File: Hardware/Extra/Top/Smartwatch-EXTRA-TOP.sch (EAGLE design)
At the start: 69 parts, among them SW6 SWITCH.MOM, SW7 SWITCH.MOM, U2 NRF52832_MODULE_MDBT42, U4 FT231XS, U5 PHOTOTRANSISTOR

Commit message: Extra features updated
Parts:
- removed C25: 1u, LinnesLab-Passives:CAPACITOR0603
- removed C26: 100n, LinnesLab-Passives:CAPACITOR0603
- removed D4: (no value), LinnesLab-DiscreteSemi:SCHOTTKY-USC
- removed LED5: RED, LinnesLab-LED:LED0603
- removed LED6: YELLOW, LinnesLab-LED:LED0603
- removed Q1: (no value), LinnesLab-DiscreteSemi:NFET-AO3404A
- removed R17: 1k, LinnesLab-Passives:RESISTOR0603
- removed SW6, SW7: SWITCH.MOM, LinnesLab-Switches:SWITCH.MOM
- removed U4: FT231XS, LinnesLab-DigitalIC:FT231XS
- added C2: 10u, LinnesLab-Passives:CAPACITOR0805
- added C27: 10p, LinnesLab-Passives:CAPACITOR0603
- added C28: 1u, LinnesLab-Passives:CAPACITOR0603
- added C29: 100n, LinnesLab-Passives:CAPACITOR0603
- added D3: (no value), LinnesLab-DiscreteSemi:SCHOTTKY-USC
- added J3: (no value), LinnesLab-Connectors:CONN_041.27MM
- added LED1: RED, LinnesLab-LED:LED0603
- added LED2: BLUE, LinnesLab-LED:LED0603
- added MIC1: (no value), LinnesLab-Electromechanical:MICROPHONE_CMC-5042PF-AC.CMEJ-0415-42-P
- added Q2: (no value), LinnesLab-DiscreteSemi:NPN-GENERIC
- added Q3: (no value), LinnesLab-DiscreteSemi:NFET-AO3404A
- added R21: 100k, LinnesLab-Passives:RESISTOR0603
- added R22, R23, R26: 10k, LinnesLab-Passives:RESISTOR0603
- added R9: 27, LinnesLab-Passives:RESISTOR0603
- added U1: NRF52832_MODULE_MDBT42, LinnesLab-Microcontrollers:NRF52832_MODULE_MDBT42
- added U6: MCP9808-MSOP8, LinnesLab-Sensors:MCP9808-MSOP8
- C1: value 4.7u -> 1u
- C10, C11: value 300p -> 2.2uF; device LinnesLab-Passives:CAPACITOR0603 -> LinnesLab-Passives:CAPACITOR0402
- C12: value 10u -> 2.2uF; device LinnesLab-Passives:CAPACITOR0805 -> LinnesLab-Passives:CAPACITOR0402
- C13, C18: value 2.2uF -> 100n; device LinnesLab-Passives:CAPACITOR0402 -> LinnesLab-Passives:CAPACITOR0603
- C14: value 100n -> 4.7u
- C15, C17: value 2.2uF -> 47p; device LinnesLab-Passives:CAPACITOR0402 -> LinnesLab-Passives:CAPACITOR0603
- C16: value 10uF -> 1u
- C19: value 2.2uF -> 1u; device LinnesLab-Passives:CAPACITOR0402 -> LinnesLab-Passives:CAPACITOR0603
- C20: value 2.2u -> 4.7u
- C22: value 47p -> 2.2u
- C23: value 47p -> 100n
- C24: value 10p -> 100n
- C3: value 4.7u -> (none)
- C4: value 100n -> (none)
- C5, C6: value 1u -> 300p
- C7: value 1u -> 10uF
- C8, C9: value (none) -> 2.2uF; device LinnesLab-Passives:CAPACITOR0603 -> LinnesLab-Passives:CAPACITOR0402
- J1: device LinnesLab-Connectors:CONN_07 -> LinnesLab-Connectors:CONN_07-1.27MM
- LED4: value BLUE -> YELLOW
- R11: value (none) -> 4.7k
- R15: value 10k -> 1k
- R16: value 27 -> 1k
- R18: value 1k -> 10k
- R6: value 10k -> 390k
- R7: value 390k -> 10k
- U2: value NRF52832_MODULE_MDBT42 -> (none); device LinnesLab-Microcontrollers:NRF52832_MODULE_MDBT42 -> LinnesLab-Displays:DISP_OLED_UG-2864HSWEG01-NO-WRAPAROUND
- U3: value (none) -> FT231XS; device LinnesLab-Displays:DISP_OLED_UG-2864HSWEG01-NO-WRAPAROUND -> LinnesLab-DigitalIC:FT231XS
- renumbered CHRG2 to CHRG1, CORTEX1 to DEBUG1, JP2 to JP1, L2 to L1, LDO2 to LDO1, SW3 to SW1, USB2 to USB1, XTAL2 to XTAL1
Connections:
- removed net A0/LIGHT: C20.1, R19.2, U2.P0.02/AIN0, U5.E
- removed net D11/SW1: SW7.1, U2.P0.11
- removed net D15/SW2: SW6.1, U2.P0.15
- removed net D29/LED.CTRL: J1.6, U2.P0.29/AIN5
- removed net D5/MOTOR: Q1.G, R15.2, U2.P0.05/AIN3
- removed net N$21: SW7.3, SW7.4
- removed net N$22: SW6.3, SW6.4
- new net A0/MICROPHONE: Q2.C, R21.2, R22.1, U1.P0.02/AIN0
- new net A5/LIGHT: C22.1, R18.2, U1.P0.29/AIN5, U5.E
- new net ALERT: R26.1, U6.ALERT
- new net D11/MOTOR: Q3.G, R19.2, U1.P0.11
- new net D15/LED.CTRL: J1.6, U1.P0.15
- new net D5/CD1: U1.P0.05/AIN3
- new net N$19: C23.1, MIC1.+, R23.1
- new net N$20: C23.2, Q2.B, R21.1
- net !CTS: now also U3.!CTS; no longer U4.!CTS
- net !DTR: now also U3.!DTR; no longer U4.!DTR
- net 3.3V: now also C11.2, C18.2, C19.1, C2.2, C24.1, C27.2, C28.1, C29.1, D5.C, J3.2, LED3.A, LED4.A, R12.2, R22.2, R23.2, R26.2, R7.2, U1.VDD, U2.VBAT, U3.!RESET, U3.VCCIO, U6.VDD; no longer C17.2, C19.2, C24.2, C25.1, C26.1, C4.2, C6.1, D2.C, LED5.A, LED6.A, R5.2, R8.2, U3.VBAT, U3.VDD, U4.!RESET, U4.VCCIO
- net A4/BATT: now also U1.P0.28/AIN4; no longer U2.P0.28/AIN4
- net A6/TIA: now also U1.P0.30/AIN6; no longer U2.P0.30/AIN6
- net A7/PPG: now also U1.P0.31/AIN7; no longer U2.P0.31/AIN7
- net D16/CS.OLED: now also U1.P0.16, U2./CS; no longer U2.P0.16, U3./CS
- net D27/CHRG.STAT: now also R8.1, U1.P0.27; no longer R12.1, U2.P0.27
- net D3/RESET.OLED: now also U1.P0.03/AIN1, U2./RES; no longer U2.P0.03/AIN1, U3./RES
- net D4/DC.OLED: now also U1.P0.04/AIN2, U2.DC/I2C_SA0; no longer U2.P0.04/AIN2, U3.DC/I2C_SA0
- net D7/SD.CS: now also U1.P0.07; no longer U2.P0.07
- net DFU: now also U1.P0.20; no longer U2.P0.20
- net DTR: now also C13.1; no longer C14.1
- net FRST: now also U1.P0.22; no longer U2.P0.22
- net FT3V3: now also U3.3V3OUT; no longer U4.3V3OUT
- net GND: now also C1.2, C11.1, C14.1, C15.1, C17.2, C19.2, C2.1, C24.2, C28.2, C29.2, C3.1, C4.2, C5.2, C7.1, C9.1, J3.1, LED1.C, LED2.C, MIC1.-, Q2.E, Q3.S, R12.1, R18.1, R5.1, R6.2, U1.GND@1, U1.GND@2, U1.GND@3, U1.GND@4, U2.BS0, U2.BS2, U2.NC(GND)@1, U2.NC(GND)@2, U2.VLSS, U2.VSS, U3.GND@16, U3.GND@6, U6.A0, U6.A1, U6.A2, U6.GND; no longer C1.1, C10.2, C11.2, C17.1, C19.1, C23.1, C25.2, C26.2, C3.2, C4.1, C5.1, C7.2, C8.1, C9.2, LED3.C, LED4.C, Q1.S, R15.1, R6.1, R7.2, R8.1, U2.GND@1, U2.GND@2, U2.GND@3, U2.GND@4, U3.BS0, U3.BS2, U3.NC(GND)@1, U3.NC(GND)@2, U3.VLSS, U3.VSS, U4.GND@16, U4.GND@6
- net LED1: now also U1.P0.17; no longer U2.P0.17
- net LED2: now also U1.P0.19; no longer U2.P0.19
- net MISO: now also U1.P0.14; no longer U2.P0.14
- net MOSI: now also U1.P0.13, U2.D1/SPI_SDIN/I2C_SDA; no longer U2.P0.13, U3.D1/SPI_SDIN/I2C_SDA
- net N$1: now also R5.2, U2.BS1; no longer R6.2, U3.BS1
- net N$10: now also LED2.A; no longer LED4.A
- net N$11: now also U1.DCC; no longer U2.DCC
- net N$12: now also C1.1, U1.DEC4; no longer C7.1, U2.DEC4
- net N$13: now also C7.2, U2.VCC; no longer C16.2, U3.VCC
- net N$15: now also C9.2, U2.VCOMH; no longer C18.2, U3.VCOMH
- net N$18: now also C27.1, D5.A, Q3.D; no longer C24.1, D2.A, Q1.D
- net N$2: now also R6.1, U2.IREF; no longer R7.1, U3.IREF
- net N$25: now also R9.2, U3.USBDM; no longer R10.2, U4.USBDM
- net N$26: now also R10.2, U3.USBDP; no longer R16.2, U4.USBDP
- net N$27: now also LED3.C, R15.2; no longer LED5.C, R17.2
- net N$28: now also LED4.C, R16.2; no longer LED6.C, R18.2
- net N$3: now also C10.2, U2.C2P; no longer C13.2, U3.C2P
- net N$4: now also C3.2, U1.P0.00/XL1; no longer C8.2, U2.P0.00/XL1
- net N$5: now also C10.1, U2.C2N; no longer C13.1, U3.C2N
- net N$6: now also C4.1, U1.P0.01/XL2; no longer C9.1, U2.P0.01/XL2
- net N$7: now also C8.2, U2.C1P; no longer C15.2, U3.C1P
- net N$8: now also C8.1, U2.C1N; no longer C15.1, U3.C1N
- net N$9: now also LED1.A; no longer LED3.A
- net P0.09/NFC1: now also C5.1, U1.P0.09; no longer C11.1, U2.P0.09
- net P0.10/NFC2: now also C6.1, U1.P0.10; no longer C10.1, U2.P0.10
- net RESET: now also C13.2, R7.1, U1.P0.21/RESET; no longer C14.2, R5.1, U2.P0.21/RESET
- net RXD: now also U1.P0.08, U3.RXD; no longer U2.P0.08, U4.RXD
- net RXLED: now also R15.1, U3.CBUS1; no longer R17.1, U4.CBUS1
- net SCK: now also U1.P0.12, U2.D0/SPI_SCLK/I2C_SCK; no longer U2.P0.12, U3.D0/SPI_SCLK/I2C_SCK
- net SCL: now also J3.3, U1.P0.26, U6.SCL; no longer U2.P0.26
- net SDA: now also J3.4, U1.P0.25, U6.SDA; no longer U2.P0.25
- net SWCLK: now also U1.SWDCLK; no longer U2.SWDCLK
- net SWDIO: now also U1.SWDIO; no longer U2.SWDIO
- net SWO: now also U1.P0.18/SWO; no longer U2.P0.18/SWO
- net TXD: now also U1.P0.06, U3.TXD; no longer U2.P0.06, U4.TXD
- net TXLED: now also R16.1, U3.CBUS2; no longer R18.1, U4.CBUS2
- net USB+: now also C17.1, R10.1; no longer C22.1, R16.1
- net USB-: now also C15.2, R9.1; no longer C23.2, R10.1
- net VIN: now also C14.2, C16.2, D2.C, D3.C, R8.2; no longer C1.2, C5.2, D4.C, D5.C, R12.2
- net VLIPO: now also C20.1, D2.A; no longer C3.1, D4.A
- net V_USB: now also D3.A, U3.VCC; no longer D5.A, U4.VCC
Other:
- note added: "I2C Adress: A0,A1,A2 connected to ground: 0x18 Other addresses: 0x19 to 0x1F"
- moved on the sheet: C1, C10, C11, C12, C13, C14, C15, C16, C17, C18, C19, C20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

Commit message: Extra Silkscreens updated
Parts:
- U1: SPICEPREFIX (none) -> X

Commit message: Microphone Removed,Silkscreen Updated, Bom Updated
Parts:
- removed C23: 100n, LinnesLab-Passives:CAPACITOR0603
- removed MIC1: (no value), LinnesLab-Electromechanical:MICROPHONE_CMC-5042PF-AC.CMEJ-0415-42-P
- removed Q2: (no value), LinnesLab-DiscreteSemi:NPN-GENERIC
- removed R21: 100k, LinnesLab-Passives:RESISTOR0603
- removed R22, R23: 10k, LinnesLab-Passives:RESISTOR0603
- added J4: (no value), LinnesLab-Connectors:CONN_03.50MIL
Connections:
- removed net A0/MICROPHONE: Q2.C, R21.2, R22.1, U1.P0.02/AIN0
- removed net D5/CD1: U1.P0.05/AIN3
- removed net D7/SD.CS: U1.P0.07
- removed net N$19: C23.1, MIC1.+, R23.1
- removed net N$20: C23.2, Q2.B, R21.1
- new net A.IN: J4.1, U1.P0.02/AIN0
- new net B.IN: J4.3, U1.P0.07
- new net MOM.BUTTON: J4.2, U1.P0.05/AIN3
- net 3.3V: no longer R22.2, R23.2
- net GND: no longer MIC1.-, Q2.E
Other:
- note added: "Ambient Light Sensor"
- note added: "Temperature Sensor"
- note added: "Vibration Motor"
- note removed: "Buttons"
- moved on the sheet: C22, C24, C27, C28, C29, D5, M1, Q3, R18, R19, R26, U5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

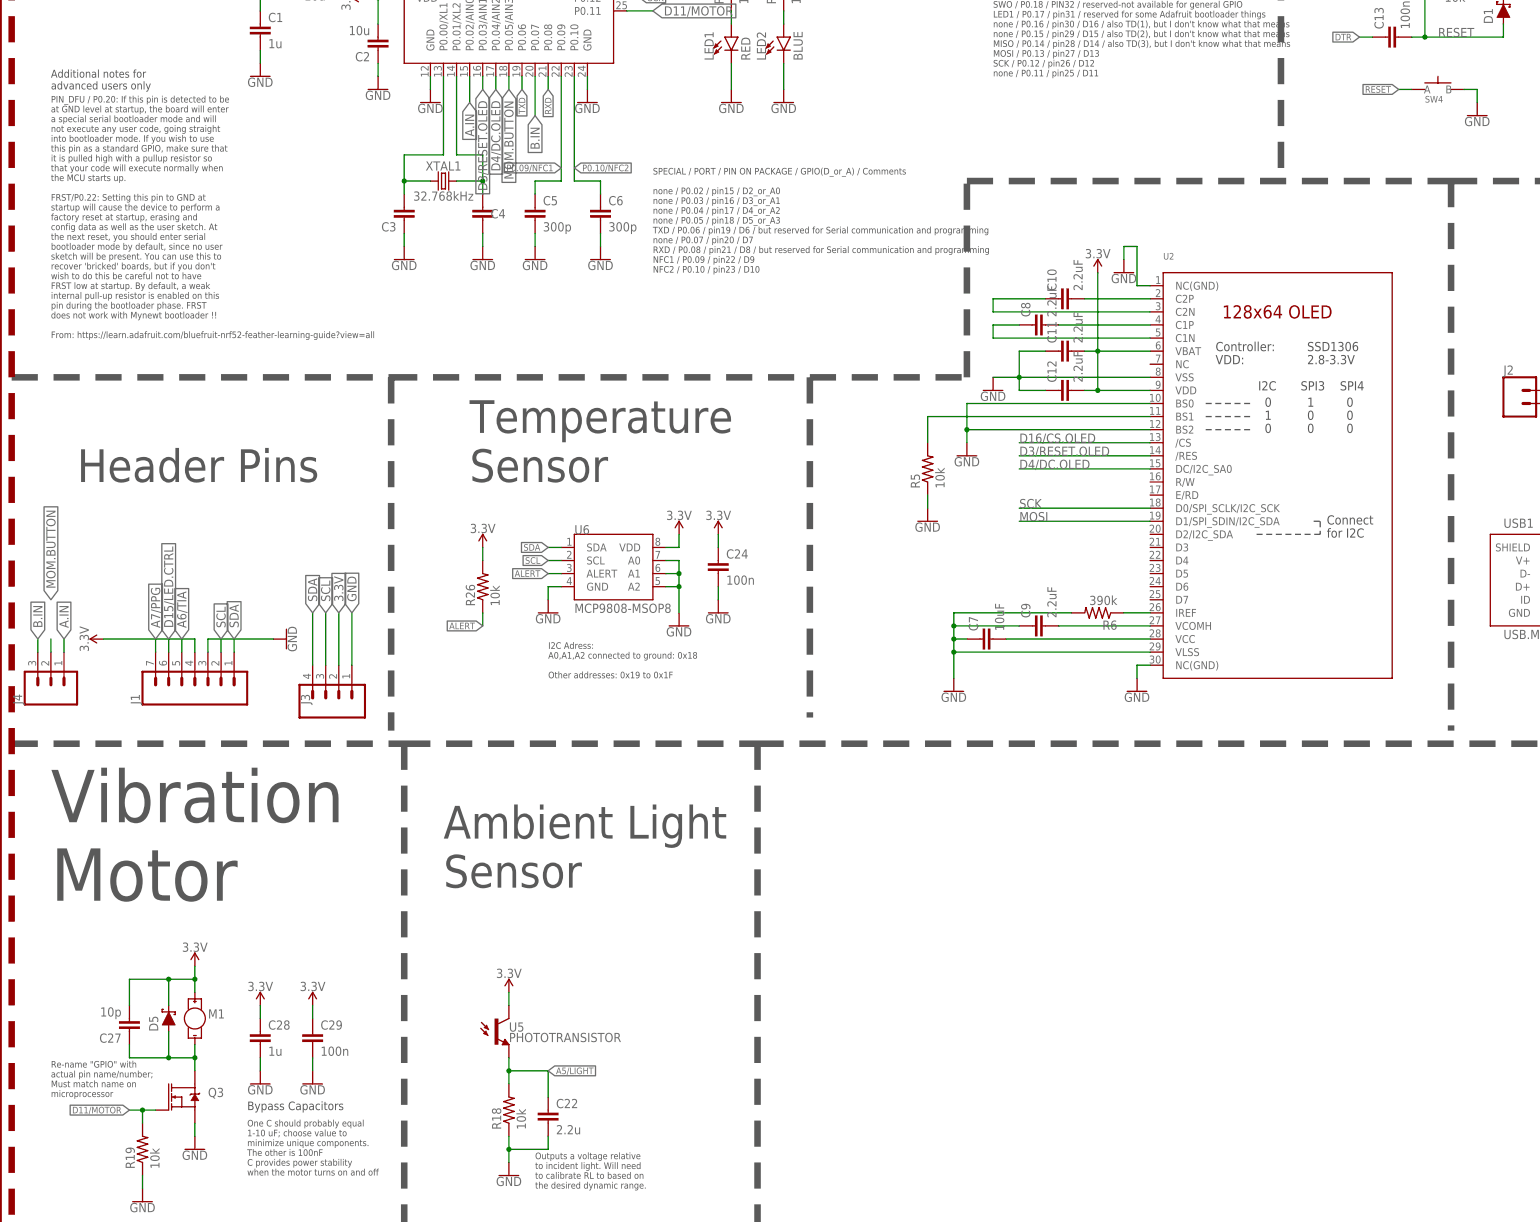
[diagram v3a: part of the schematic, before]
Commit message: BOMs finished
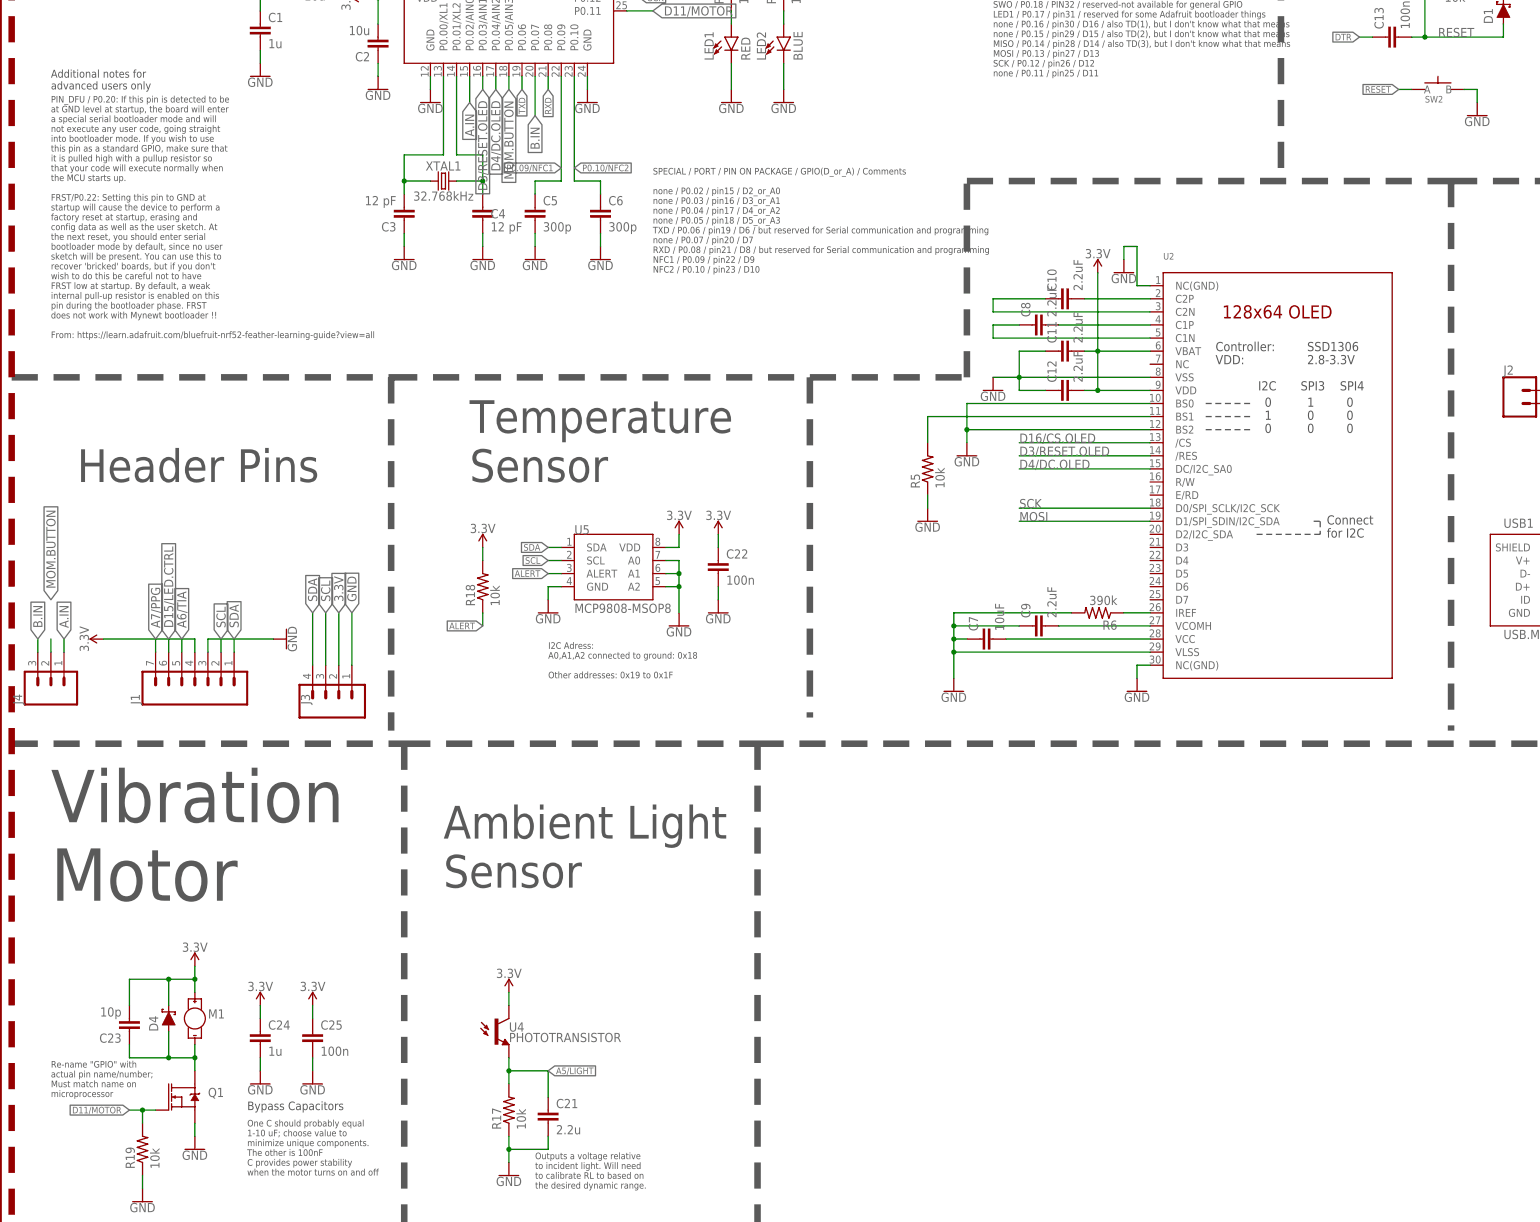
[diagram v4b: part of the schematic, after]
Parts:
- removed C28: 1u, LinnesLab-Passives:CAPACITOR0603
- removed R26: 10k, LinnesLab-Passives:RESISTOR0603
- removed U6: MCP9808-MSOP8, LinnesLab-Sensors:MCP9808-MSOP8
- added C21: 2.2u, LinnesLab-Passives:CAPACITOR0603
- added R17: 10k, LinnesLab-Passives:RESISTOR0603
- added U4: PHOTOTRANSISTOR, LinnesLab-Sensors:PHOTOTRANSISTOR
- C22: value 2.2u -> 100n
- C24: value 100n -> 1u
- C3, C4: value (none) -> 12 pF
- U5: value PHOTOTRANSISTOR -> MCP9808-MSOP8; device LinnesLab-Sensors:PHOTOTRANSISTOR -> LinnesLab-Sensors:MCP9808-MSOP8; SPICEPREFIX (none) -> X
- renumbered C27 to C23, C29 to C25, D5 to D4, Q3 to Q1, SW4 to SW2
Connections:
- net 3.3V: now also C22.1, R18.2, U4.C, U5.VDD; no longer C28.1, R26.2, U5.C, U6.VDD
- net A5/LIGHT: now also C21.1, R17.2, U4.E; no longer C22.1, R18.2, U5.E
- net ALERT: now also R18.1, U5.ALERT; no longer R26.1, U6.ALERT
- net GND: now also C21.2, R17.1, U5.A0, U5.A1, U5.A2, U5.GND; no longer C28.2, R18.1, U6.A0, U6.A1, U6.A2, U6.GND
- net SCL: now also U5.SCL; no longer U6.SCL
- net SDA: now also U5.SDA; no longer U6.SDA
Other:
- moved on the sheet: C22, C24, R18

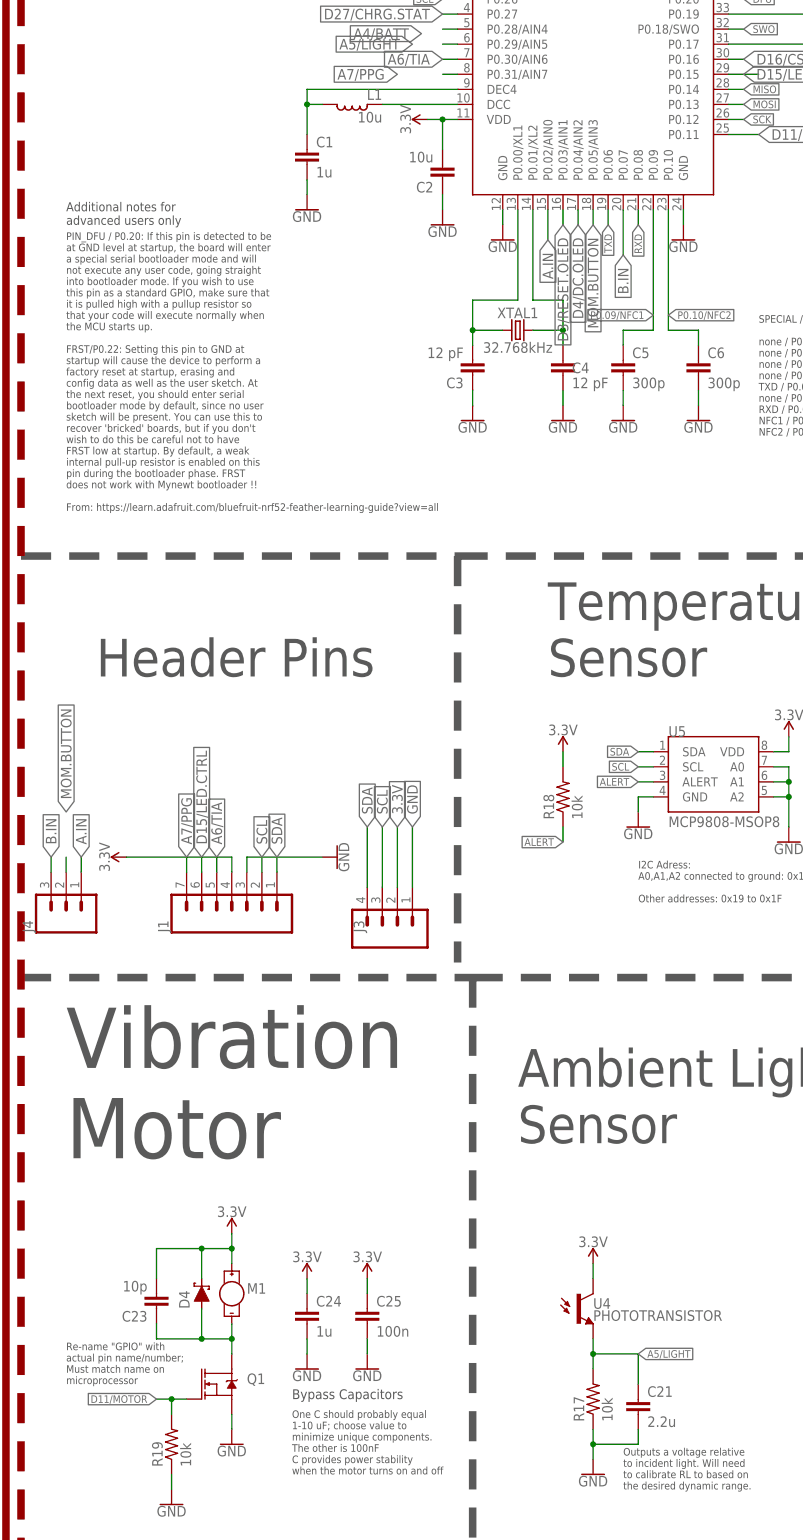
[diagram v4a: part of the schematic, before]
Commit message: Encoder changed, BOMs updated
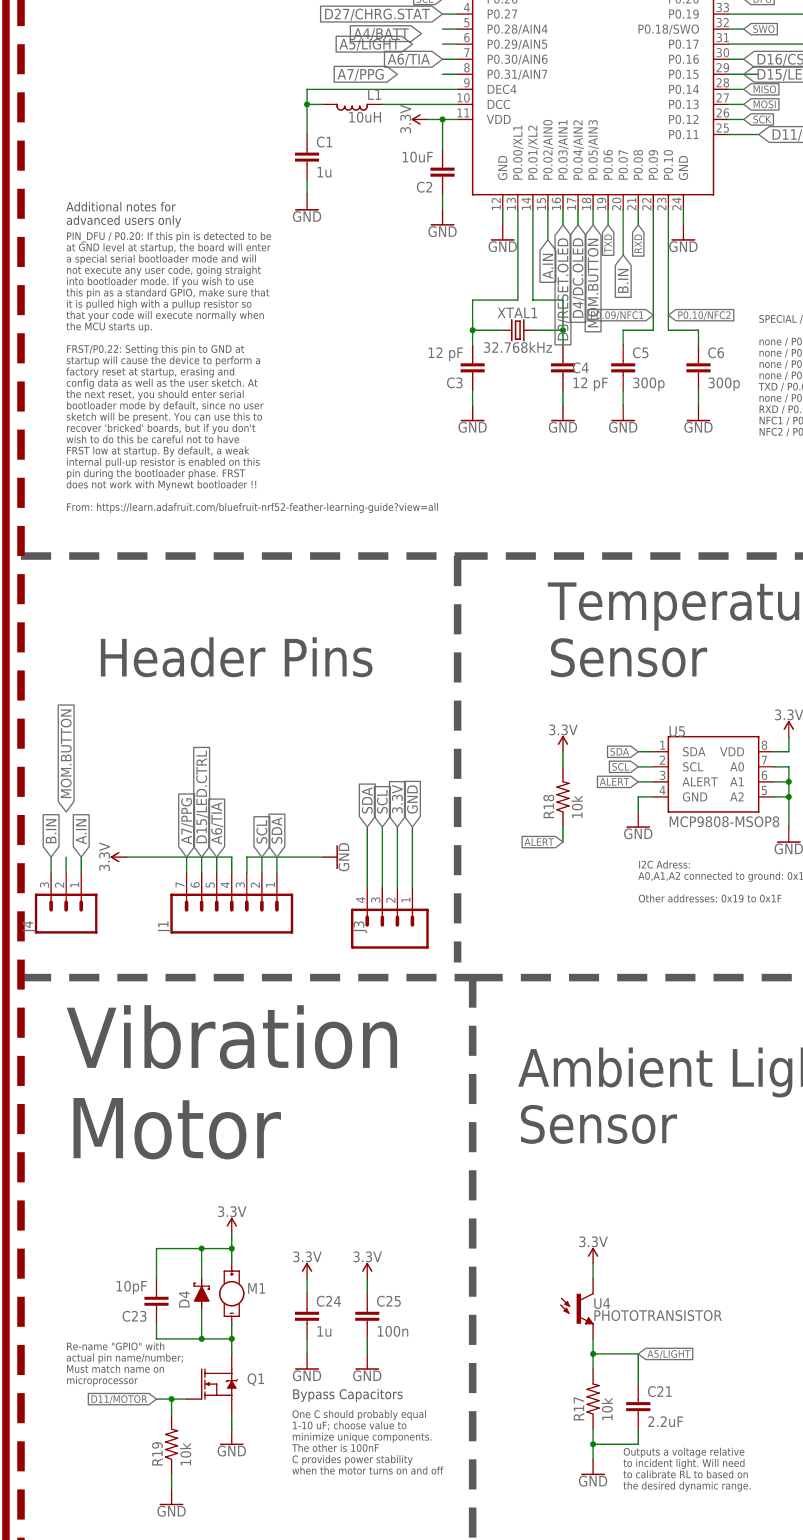
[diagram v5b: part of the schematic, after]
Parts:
- C2: value 10u -> 10uF
- C21: value 2.2u -> 2.2uF
- C23: value 10p -> 10pF
- L1: value 10u -> 10uH
